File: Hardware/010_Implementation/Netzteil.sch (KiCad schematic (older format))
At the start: 18 parts, among them U1 TPS62163DGK

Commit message: Board Version 5
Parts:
- removed U1: TPS62163DGK, Package_SO:VSSOP-8_3.0x3.0mm_P0.65mm, symbol Regulator_Switching:TPS62163DSG
- added U1: TPS62170DGK, Package_SO:VSSOP-8_3.0x3.0mm_P0.65mm, symbol Board:TPS62170DGK
- C1: value 10n -> 100n; footprint Capacitor_SMD:C_0603_1608Metric_Pad1.05x0.95mm_HandSolder -> Capacitor_SMD:C_0603_1608Metric_Pad1.08x0.95mm_HandSolder
- C10: value C -> 100n; footprint (none) -> Capacitor_SMD:C_0603_1608Metric_Pad1.08x0.95mm_HandSolder
- C16: footprint (none) -> Capacitor_SMD:C_1206_3216Metric_Pad1.33x1.80mm_HandSolder
- C2, C3: footprint Capacitor_SMD:C_0603_1608Metric_Pad1.05x0.95mm_HandSolder -> Capacitor_SMD:C_1206_3216Metric_Pad1.33x1.80mm_HandSolder
- C9: footprint Capacitor_SMD:C_0603_1608Metric_Pad1.05x0.95mm_HandSolder -> Capacitor_SMD:C_0603_1608Metric_Pad1.08x0.95mm_HandSolder
- D8: value D -> SMAJ16A; footprint (none) -> Diode_SMD:D_SMA; Vorhanden (none) -> Yes
- F1: value Fuse -> R452002; footprint (none) -> Fuse:Fuse_2512_6332Metric_Pad1.52x3.35mm_HandSolder; Vorhanden (none) -> Yes
- FB1, FB2: footprint (none) -> Inductor_SMD:L_0603_1608Metric_Pad1.05x0.95mm_HandSolder
- L3: Vorhanden (none) -> Yes
- R1, R2, R3: footprint Resistor_SMD:R_0805_2012Metric_Pad1.15x1.40mm_HandSolder -> Resistor_SMD:R_0603_1608Metric_Pad0.98x0.95mm_HandSolder
- R19, R20: footprint (none) -> Resistor_SMD:R_0603_1608Metric_Pad0.98x0.95mm_HandSolder; NP (none) -> NP
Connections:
- net GND: now also U1.1 (PGND), U1.4 (AGND)
- net at C3.1, FB2.2, L1.2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: now also U1.6 (VOS)
- net at R19.2, R20.1: now also U1.5 (FB)
- net at C2.1, FB1.1: now also U1.2 (VIN), U1.3 (EN)
- net at L1.1: now also U1.7 (SW)
- net at R3.2: now also U1.8 (PG)
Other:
- note added: "180kOm for Adjustable Version. 0Ohm for fixed 5V\n"
- moved on the sheet: C1, C10, C16, C2, C3, C9, D8, F1, FB1, FB2, L1, L3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

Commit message: Board Version 6
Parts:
- L1: footprint Capacitor_SMD:C_0603_1608Metric_Pad1.05x0.95mm_HandSolder -> Board:INDPM5550X300N
- L3: footprint (none) -> Board:INDPM5550X300N
- U1: value TPS62170DGK -> TPS62160DGK
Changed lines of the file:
@@
 F 0 "L1" V 7325 3200 50  0000 C CNN
 F 1 "2.2u" V 7234 3200 50  0000 C CNN
-F 2 "Capacitor_SMD:C_0603_1608Metric_Pad1.05x0.95mm_HandSolder" H 7135 3200 50  0001 C CNN
+F 2 "Board:INDPM5550X300N" H 7135 3200 50  0001 C CNN
 F 3 "~" H 7135 3200 50  0001 C CNN
 	1    7135 3200
@@
 F 0 "L3" V 2709 3200 50  0000 C CNN
 F 1 "5u" V 2800 3200 50  0000 C CNN
-F 2 "" H 2890 3200 50  0001 C CNN
+F 2 "Board:INDPM5550X300N" H 2890 3200 50  0001 C CNN
 F 3 "~" H 2890 3200 50  0001 C CNN
 F 4 "Yes" H 2890 3200 50  0001 C CNN "Vorhanden"
@@
 P 6460 2950
 F 0 "U1" H 6460 2967 50  0000 C CNN
-F 1 "TPS62170DGK" H 6460 2876 50  0000 C CNN
+F 1 "TPS62160DGK" H 6460 2876 50  0000 C CNN
 F 2 "Package_SO:VSSOP-8_3.0x3.0mm_P0.65mm" H 6210 2850 50  0001 C CNN
 F 3 "" H 6210 2850 50  0001 C CNN

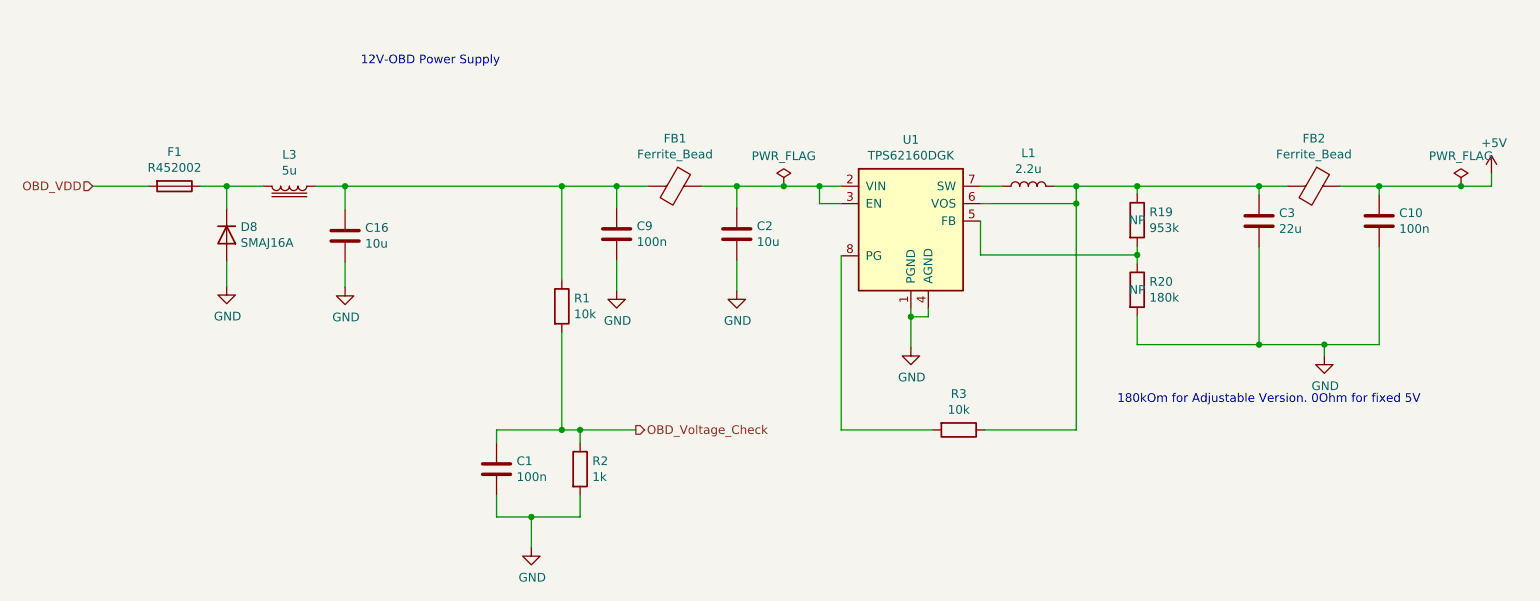
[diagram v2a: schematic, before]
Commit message: Changed Resistor values on voltage regulator
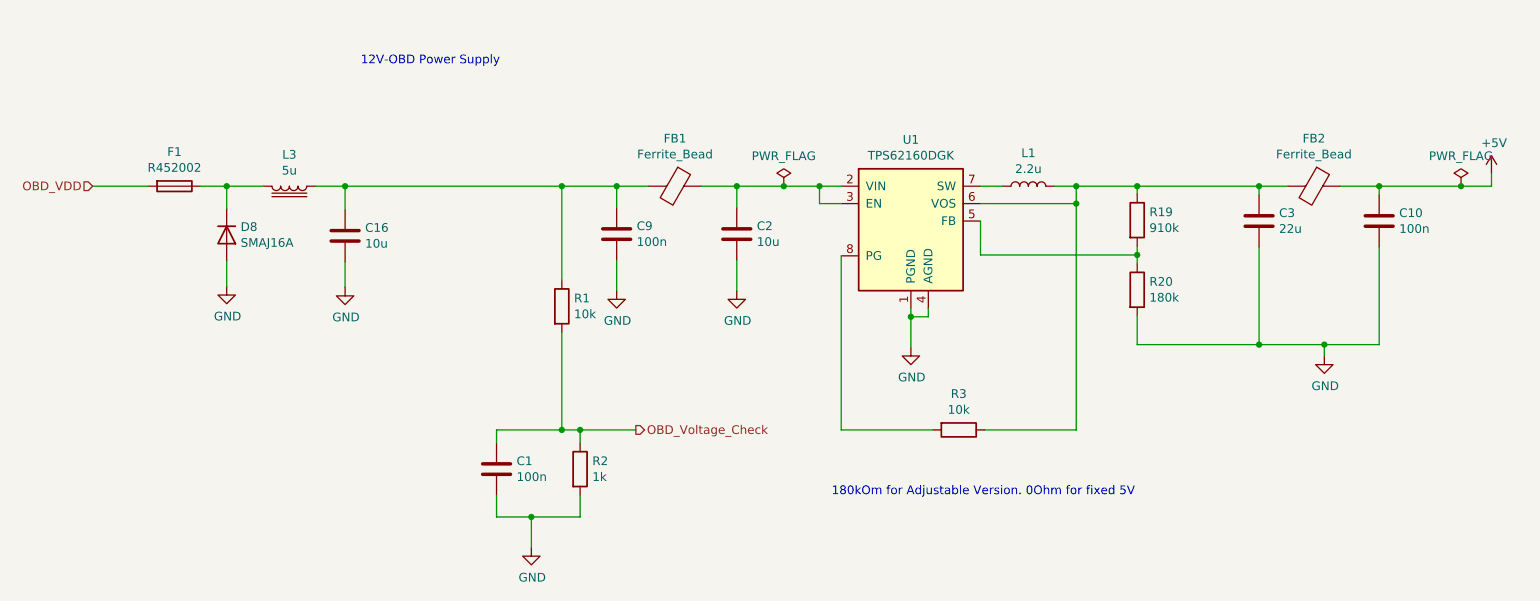
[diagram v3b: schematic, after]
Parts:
- R19: value 953k -> 910k
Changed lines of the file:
@@
 F 2 "Resistor_SMD:R_0603_1608Metric_Pad0.98x0.95mm_HandSolder" V 7690 3795 50  0001 C CNN
 F 3 "~" H 7760 3795 50  0001 C CNN
-F 4 "NP" H 7760 3795 50  0000 C CNN "NP"
+F 4 "NP" H 7760 3795 50  0001 C CNN "NP"
 	1    7760 3795
 	1    0    0    -1
@@
 P 7760 3395
 F 0 "R19" H 7830 3441 50  0000 L CNN
-F 1 "953k" H 7830 3350 50  0000 L CNN
+F 1 "910k" H 7830 3350 50  0000 L CNN
 F 2 "Resistor_SMD:R_0603_1608Metric_Pad0.98x0.95mm_HandSolder" V 7690 3395 50  0001 C CNN
 F 3 "~" H 7760 3395 50  0001 C CNN
-F 4 "NP" H 7760 3395 50  0000 C CNN "NP"
+F 4 "NP" H 7760 3395 50  0001 C CNN "NP"
 	1    7760 3395
 	1    0    0    -1
@@
 Wire Wire Line
 	8835 4110 9150 4110
-Text Notes 7645 4455 0    50   ~ 0
+Text Notes 6005 4985 0    50   ~ 0
 180kOm for Adjustable Version. 0Ohm for fixed 5V\n
 $Comp
